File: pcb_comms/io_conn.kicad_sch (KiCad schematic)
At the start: 24 parts, among them IC1 CP2102N-A02-GQFN28, J1 Conn_01x06_Pin, J3 OBC_I2C, J4 Conn_01x04, J5 OBC_I2C, J6 Conn_01x04, J7 105164-0001, U6 ADP122AUJZ-3.3-R7

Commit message: Version 1.0. No DRA yet
From now on I will make the connections for IIS and then adapt it for the club
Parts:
- C39: value 10uF/25V(20%) -> 10uF
- R9: value 1k -> 1K
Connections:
- net GND: no longer J3.2 (Pin_2)
- new net OCP_NFAULT: J3.2 (Pin_2)
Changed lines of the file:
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@@
 	(wire
 		(pts
-			(xy 226.06 76.2) (xy 233.68 76.2)
+			(xy 227.33 76.2) (xy 233.68 76.2)
 		)
 		(stroke
@@
 		)
 	)
+	(global_label "OCP_NFAULT"
+		(shape input)
+		(at 227.33 76.2 180)
+		(fields_autoplaced yes)
+		(effects
+			(font
+				(size 1.27 1.27)
+			)
+			(justify right)
+		)
+		(property "Intersheetrefs" "${INTERSHEET_REFS}"
+			(at 212.6728 76.2 0)
+			(effects
+				(font
+					(size 1.27 1.27)
+				)
+				(justify right)
+				(hide yes)
+			)
+		)
+	)
 	(global_label "JTDO_SWO_TO_STM32"
 		(shape input)
@@
 			)
 		)
-		(property "Value" "1k"
+		(property "Value" "1K"
 			(at 111.76 182.8799 0)
 			(effects
@@
 		(dnp no)
 		(property "Reference" "C39"
-			(at 178.308 65.278 0)
+			(at 180.34 66.04 0)
 			(effects
 				(font
@@
 			)
 		)
-		(property "Value" "10uF/25V(20%)"
-			(at 176.53 79.502 90)
-			(effects
-				(font
-					(size 0.889 0.889)
+		(property "Value" "10uF"
+			(at 180.34 68.326 0)
+			(effects
+				(font
+					(size 1.27 1.27)
 				)
 				(justify left)
@@
 					(unit 1)
 				)
-			)
-		)
-	)
-	(symbol
-		(lib_id "power:GND")
-		(at 226.06 76.2 270)
-		(unit 1)
-		(exclude_from_sim no)
-		(in_bom yes)
-		(on_board yes)
-		(dnp no)
-		(fields_autoplaced yes)
-		(property "Reference" "#PWR060"
-			(at 219.71 76.2 0)
-			(effects
-				(font
-					(size 1.27 1.27)
-				)
-				(hide yes)
-			)
-		)
-		(property "Value" "GND"
-			(at 222.25 76.1999 90)
-			(effects
-				(font
-					(size 1.27 1.27)
-				)
-				(justify right)
-			)
-		)
-		(property "Footprint" ""
-			(at 226.06 76.2 0)
-			(effects
-				(font
-					(size 1.27 1.27)
-				)
-				(hide yes)
-			)
-		)
-		(property "Datasheet" ""
-			(at 226.06 76.2 0)
-			(effects
-				(font
-					(size 1.27 1.27)
-				)
-				(hide yes)
-			)
-		)
-		(property "Description" "Power symbol creates a global label with name \"GND\" , ground"
-			(at 226.06 76.2 0)
-			(effects
-				(font
-					(size 1.27 1.27)
-				)
-				(hide yes)
-			)
-		)
-		(pin "1"
-		)
-		(instances
-			(project "pcb_comms_board"
-				(path "/ea597178-b44d-4db9-826c-8f86e8d231f0/a4d41170-f1e3-4812-89ef-2aa6a238f022"
-					(reference "#PWR060")
-					(unit 1)
-				)

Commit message: Add footprints
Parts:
- removed J3, J5: OBC_I2C, symbol Connector_Generic:Conn_01x02
- removed J4, J6: Conn_01x04, symbol Connector_Generic:Conn_01x04
- added J2: Conn_02x20_Counter_Clockwise, Connector_PinSocket_2.54mm:PinSocket_2x20_P2.54mm_Vertical, symbol Connector_Generic:Conn_02x20_Counter_Clockwise
- added J3: Conn_01x04, Connector_PinSocket_2.54mm:PinSocket_1x05_P2.54mm_Vertical, symbol Connector_Generic:Conn_01x04
- C37, C38, C39, C40, C41, C48: footprint (none) -> Capacitor_SMD:C_0805_2012Metric_Pad1.18x1.45mm_HandSolder
- C47: footprint (none) -> Capacitor_SMD:C_1210_3225Metric_Pad1.33x2.70mm_HandSolder
- CR1, CR2: footprint (none) -> SCHOTTKY_DIODE_SD1206S040S1R0:SCHOTTKY_DIODE_SD1206S040S1R0
- D2: footprint (none) -> ESD_PROTECTION_DIODE_SP0503BAHTG:ESD_PROTECTION_DIODE_SP0503BAHTG
- D6: value Green -> GREEN; footprint (none) -> LED_SMD:LED_0805_2012Metric_Pad1.15x1.40mm_HandSolder
- IC1: footprint (none) -> USB_TO_UART_BRIDGE_CP2102N:USB_TO_UART_BRIDGE_CP2102N-A02-GQFN28
- J1: footprint (none) -> Connector_PinHeader_2.54mm:PinHeader_1x06_P2.54mm_Vertical_SMD_Pin1Right
- J7: value 105164-0001 -> USB-B-Micro; footprint (none) -> USB_RECEPTACLE_105164-0001_MOLEX:USB_RECEPTACLE_105164-0001
- R2, R3, R4: footprint (none) -> Resistor_SMD:R_0805_2012Metric_Pad1.20x1.40mm_HandSolder
- R9: footprint Resistor_SMD:R_0805_2012Metric -> Resistor_SMD:R_0805_2012Metric_Pad1.20x1.40mm_HandSolder
- SB3: footprint (none) -> Jumper:SolderJumper-2_P1.3mm_Open_RoundedPad1.0x1.5mm
- U6: footprint (none) -> LDO_ADP122AUJZ_3_3_R7:UJ_5_ADI
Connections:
- net GND: now also J2.11 (Pin_11), J2.12 (Pin_12), J2.13 (Pin_13), J2.14 (Pin_14), J2.17 (Pin_17), J2.18 (Pin_18), J2.21 (Pin_21), J2.22 (Pin_22), J2.27 (Pin_27), J2.28 (Pin_28), J2.3 (Pin_3), J2.37 (Pin_37), J2.38 (Pin_38), J2.39 (Pin_39), J2.4 (Pin_4), J2.40 (Pin_40)
- net OCP_EN: now also J2.30 (Pin_30)
- net SPI1_CS: now also J2.25 (Pin_25)
- net SPI1_MISO: now also J2.23 (Pin_23)
- net SPI1_MOSI: now also J2.26 (Pin_26)
- net SPI1_SCK: now also J2.24 (Pin_24)
- net SPI2_CS: now also J3.4 (Pin_4)
- net SPI2_MISO: now also J3.3 (Pin_3)
- net SPI2_MOSI: now also J3.2 (Pin_2)
- net SPI2_SCK: now also J3.1 (Pin_1)
- net VBAT_IN: now also J2.5 (Pin_5)
- no-connect marks 19 -> 37
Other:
- note added: "TO OBC"
- note removed: "CAN BUS (SPI)"
- note removed: "OBC"

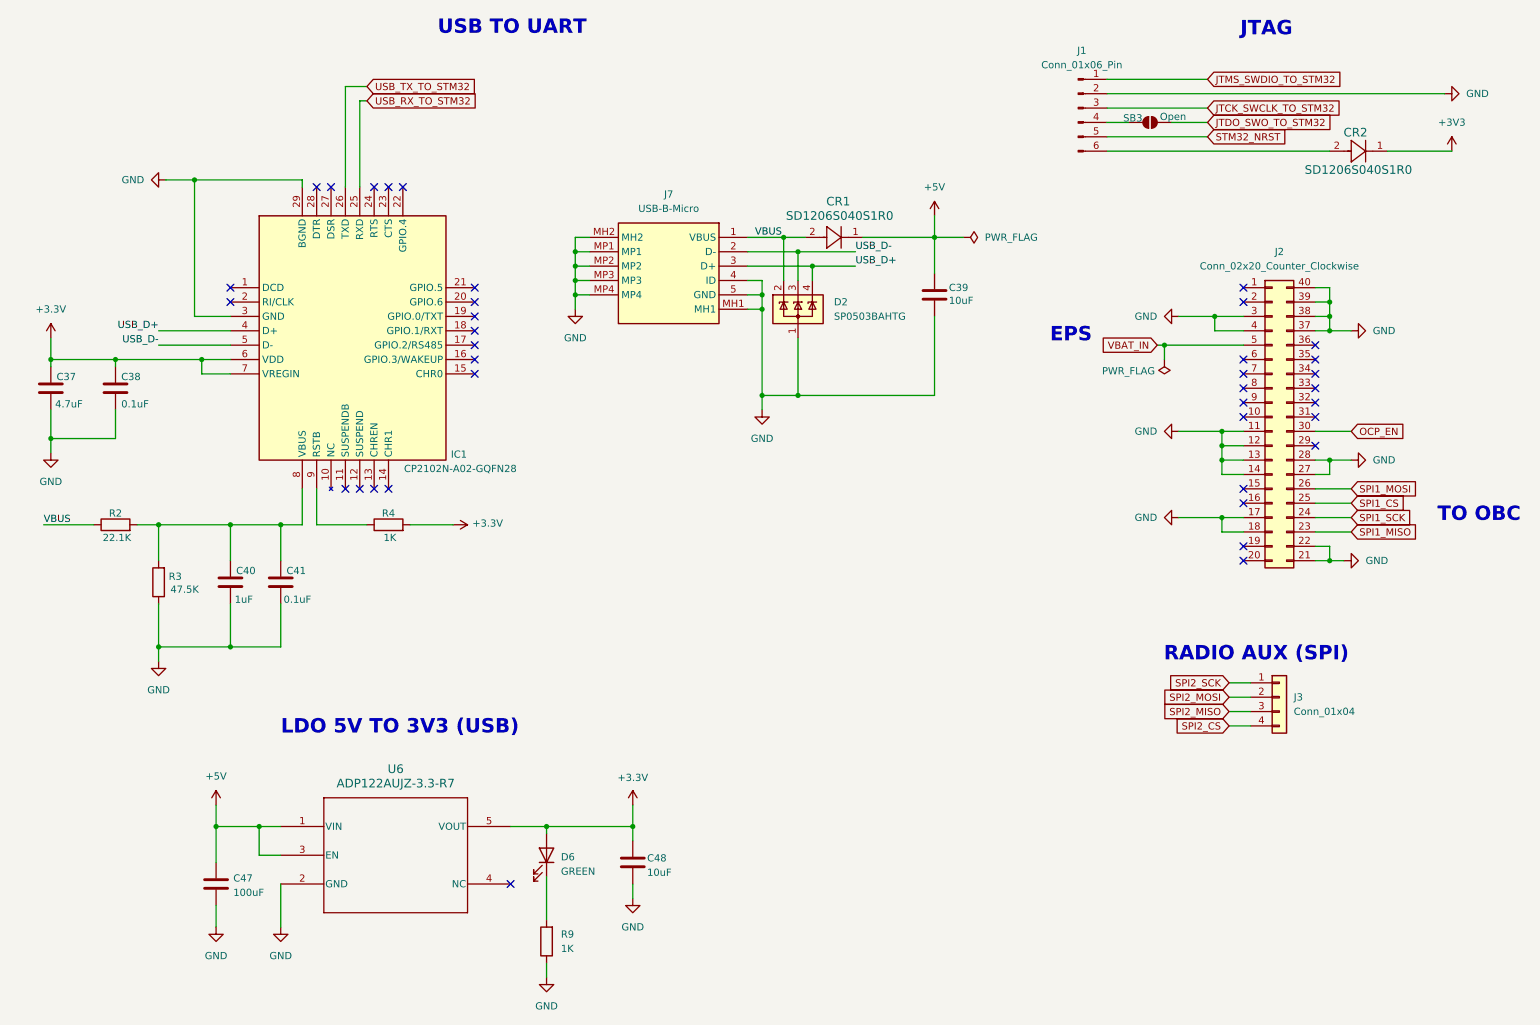
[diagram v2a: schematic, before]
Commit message: Add DRA818
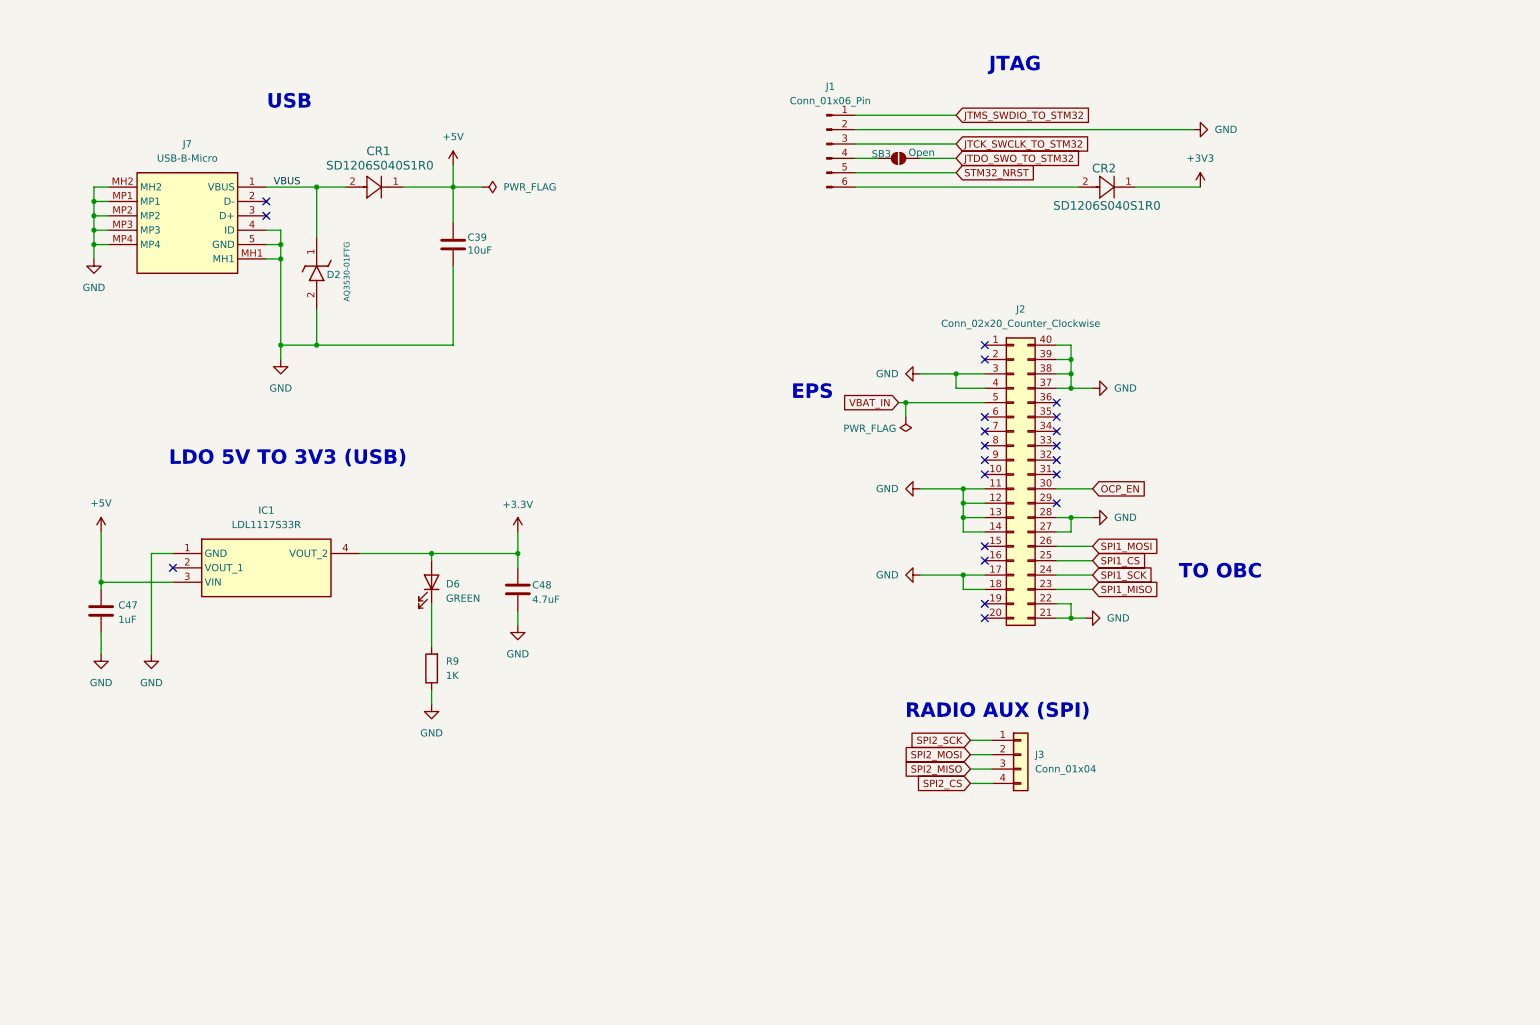
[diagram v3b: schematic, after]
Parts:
- removed C37: 4.7uF, Capacitor_SMD:C_0805_2012Metric_Pad1.18x1.45mm_HandSolder, symbol Device:C
- removed C38, C41: 0.1uF, Capacitor_SMD:C_0805_2012Metric_Pad1.18x1.45mm_HandSolder, symbol Device:C
- removed C40: 1uF, Capacitor_SMD:C_0805_2012Metric_Pad1.18x1.45mm_HandSolder, symbol Device:C
- removed D2: SP0503BAHTG, ESD_PROTECTION_DIODE_SP0503BAHTG:ESD_PROTECTION_DIODE_SP0503BAHTG, symbol Power_Protection:SP0503BAHT
- removed IC1: CP2102N-A02-GQFN28, USB_TO_UART_BRIDGE_CP2102N:USB_TO_UART_BRIDGE_CP2102N-A02-GQFN28, symbol USB_TO_UART_BRIDGE_CP2102N-A02-GQFN28:CP2102N-A02-GQFN28
- removed R2: 22.1K, Resistor_SMD:R_0805_2012Metric_Pad1.20x1.40mm_HandSolder, symbol Device:R
- removed R3: 47.5K, Resistor_SMD:R_0805_2012Metric_Pad1.20x1.40mm_HandSolder, symbol Device:R
- removed R4: 1K, Resistor_SMD:R_0805_2012Metric_Pad1.20x1.40mm_HandSolder, symbol Device:R
- removed U6: ADP122AUJZ-3.3-R7, LDO_ADP122AUJZ_3_3_R7:UJ_5_ADI, symbol LDO_ADP122AUJZ_3_3_R7:ADP122AUJZ-3.3-R7
- added D2: AQ3530-01FTG, ESD_PROTECTION_DIODE_AQ3530-01FTG:ESD_PROTECTION_DIODE_AQ3530-01FTG, symbol ESD_PROTECTION_DIODE_AQ3530-01FTG:AQ3530-01FTG
- added IC1: LDL1117S33R, LDO_LDL1117S33R:LDO_LDL1117S33R, symbol LDO_LDL1117S33R:LDL1117S33R
- C47: value 100uF -> 1uF; footprint Capacitor_SMD:C_1210_3225Metric_Pad1.33x2.70mm_HandSolder -> Capacitor_SMD:C_0805_2012Metric_Pad1.18x1.45mm_HandSolder
- C48: value 10uF -> 4.7uF
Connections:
- net +3.3V: now also IC1.4 (VOUT_2)
- net +5V: now also IC1.3 (VIN)
- net GND: now also D2.2 (A), IC1.1 (GND)
- net VBUS: now also D2.1 (K)
- net USB_D+: no longer names the net of J7.3 (D+)
- net USB_D-: no longer names the net of J7.2 (D-)
- no-connect marks 37 -> 21
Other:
- note added: "USB"
- note removed: "USB TO UART"
- moved on the sheet: C39, C47, C48, CR1, CR2, D6, J1, J2, J3, J7, R9, SB3

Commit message: remove gps
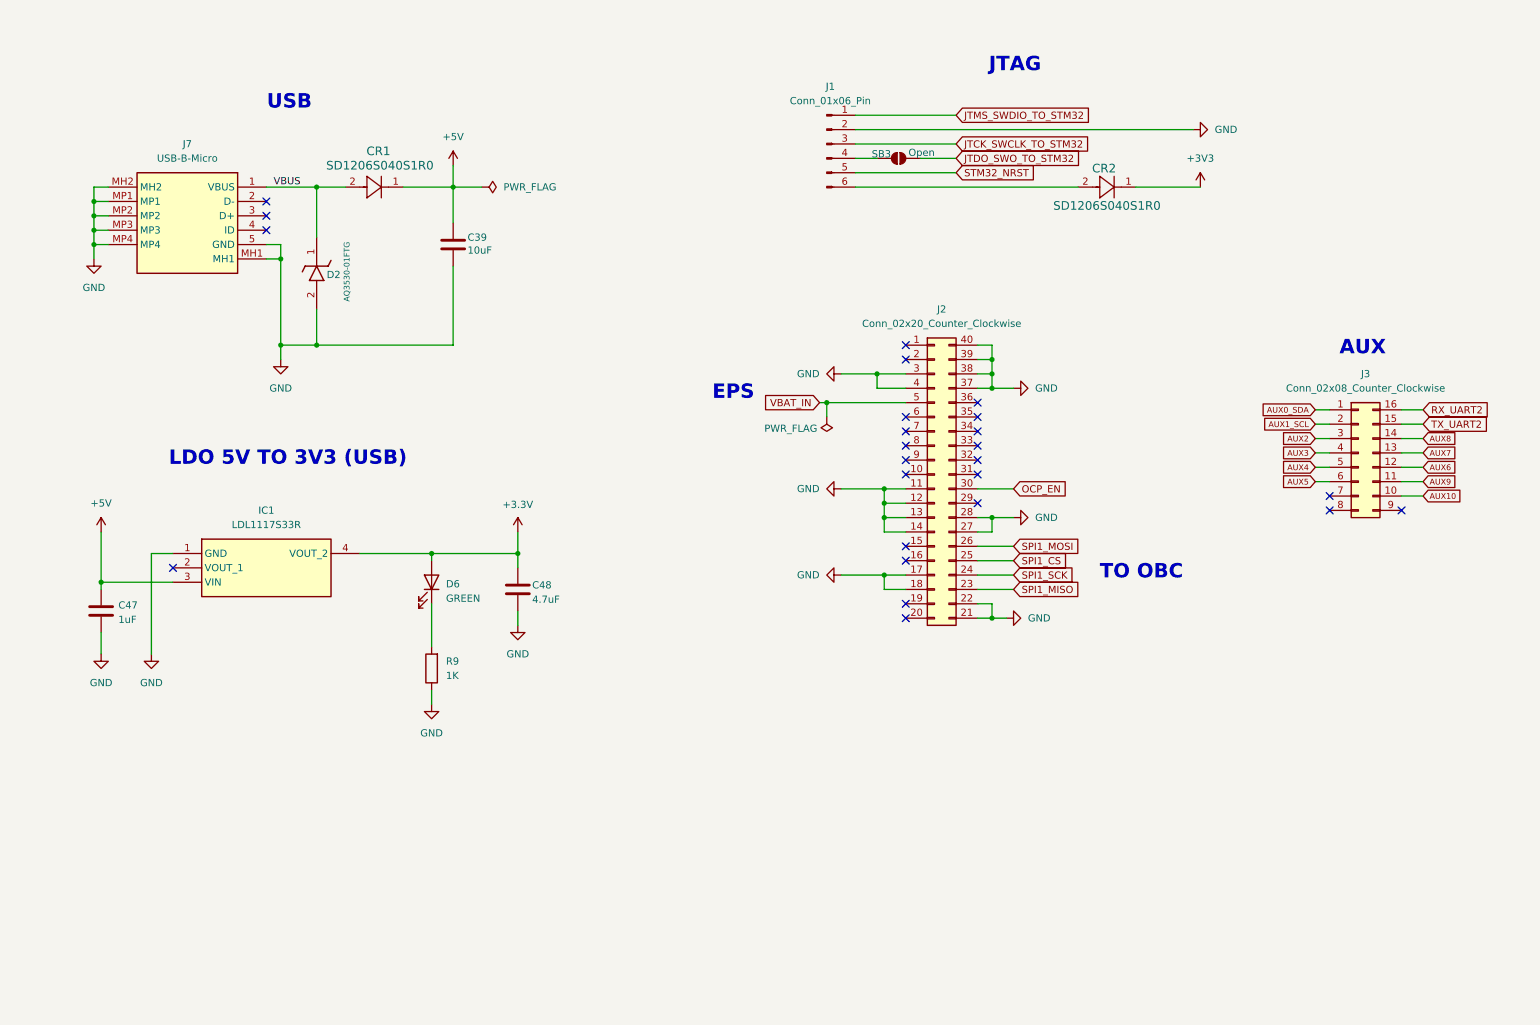
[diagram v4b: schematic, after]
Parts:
- removed J3: Conn_01x04, Connector_PinSocket_2.54mm:PinSocket_1x05_P2.54mm_Vertical, symbol Connector_Generic:Conn_01x04
- added J3: Conn_02x08_Counter_Clockwise, Connector_PinSocket_2.54mm:PinSocket_2x08_P2.54mm_Vertical_SMD, symbol Connector_Generic:Conn_02x08_Counter_Clockwise
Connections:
- net GND: no longer J7.4 (ID)
- new net AUX0_SDA: J3.1 (Pin_1)
- new net AUX10: J3.10 (Pin_10)
- new net AUX1_SCL: J3.2 (Pin_2)
- new net AUX2: J3.3 (Pin_3)
- new net AUX3: J3.4 (Pin_4)
- new net AUX4: J3.5 (Pin_5)
- new net AUX5: J3.6 (Pin_6)
- new net AUX6: J3.12 (Pin_12)
- new net AUX7: J3.13 (Pin_13)
- new net AUX8: J3.14 (Pin_14)
- new net AUX9: J3.11 (Pin_11)
- new net RX_UART2: J3.16 (Pin_16)
- new net TX_UART2: J3.15 (Pin_15)
- no-connect marks 21 -> 25
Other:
- note added: "AUX"
- note removed: "RADIO AUX (SPI)"
- moved on the sheet: J2

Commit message: Add UART USB
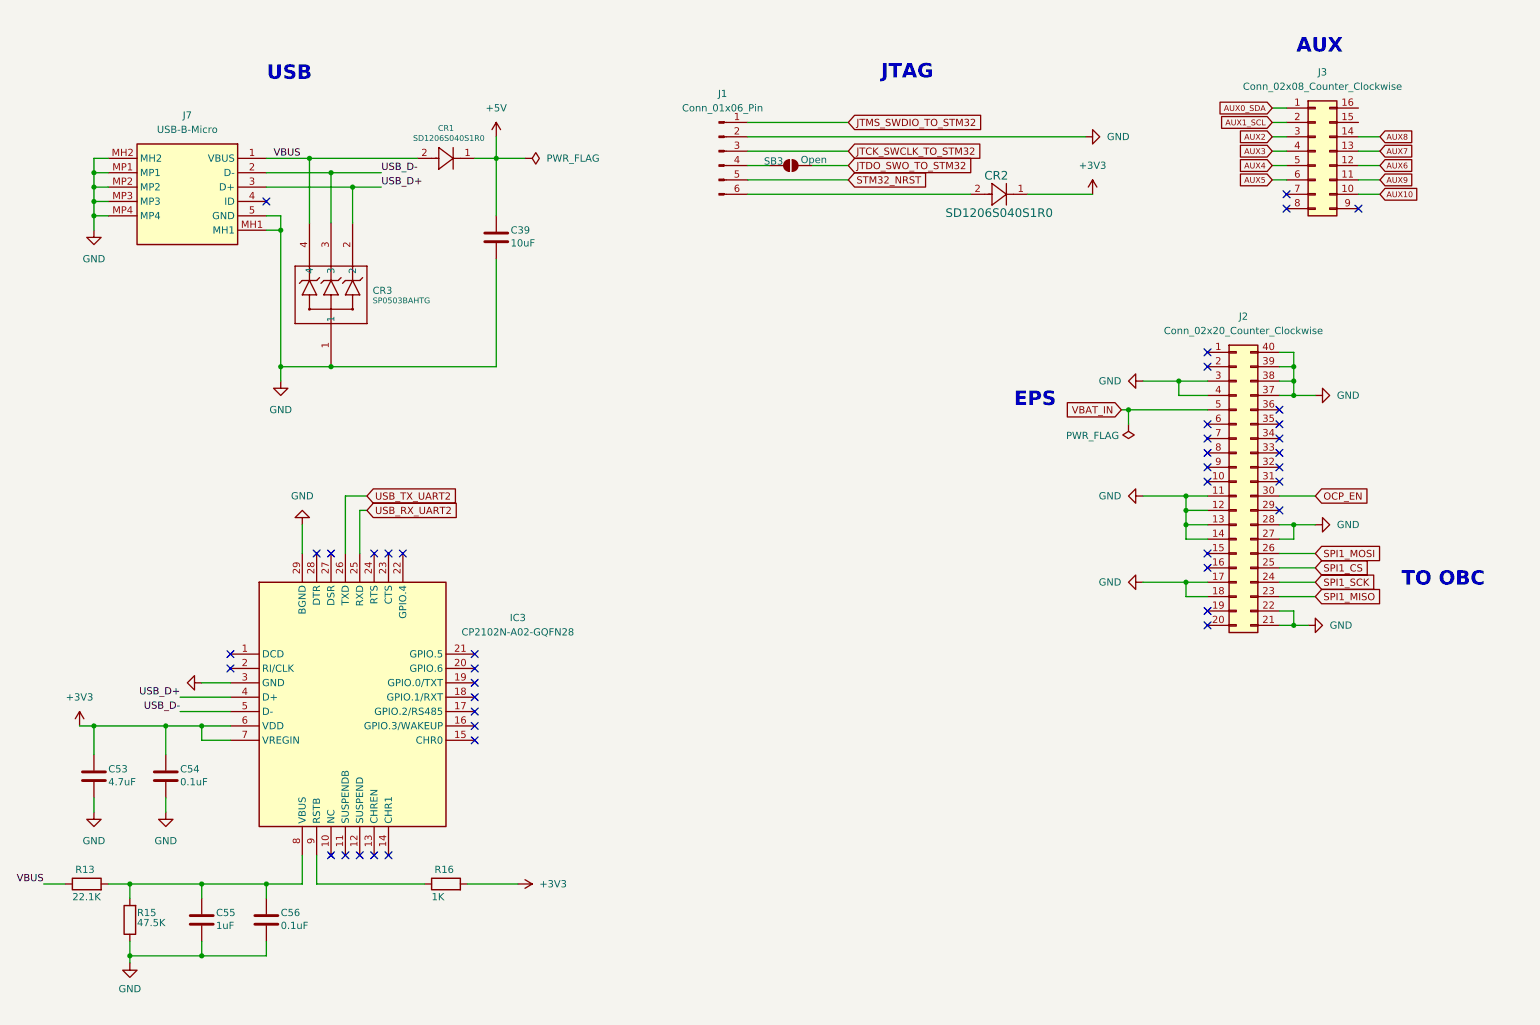
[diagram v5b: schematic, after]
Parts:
- removed C47: 1uF, Capacitor_SMD:C_0805_2012Metric_Pad1.18x1.45mm_HandSolder, symbol Device:C
- removed C48: 4.7uF, Capacitor_SMD:C_0805_2012Metric_Pad1.18x1.45mm_HandSolder, symbol Device:C
- removed D2: AQ3530-01FTG, ESD_PROTECTION_DIODE_AQ3530-01FTG:ESD_PROTECTION_DIODE_AQ3530-01FTG, symbol ESD_PROTECTION_DIODE_AQ3530-01FTG:AQ3530-01FTG
- removed D6: GREEN, LED_SMD:LED_0805_2012Metric_Pad1.15x1.40mm_HandSolder, symbol Device:LED
- removed IC1: LDL1117S33R, LDO_LDL1117S33R:LDO_LDL1117S33R, symbol LDO_LDL1117S33R:LDL1117S33R
- removed R9: 1K, Resistor_SMD:R_0805_2012Metric_Pad1.20x1.40mm_HandSolder, symbol Device:R
- added C53: 4.7uF, Capacitor_SMD:C_0805_2012Metric_Pad1.18x1.45mm_HandSolder, symbol Device:C
- added C54, C56: 0.1uF, Capacitor_SMD:C_0805_2012Metric_Pad1.18x1.45mm_HandSolder, symbol Device:C
- added C55: 1uF, Capacitor_SMD:C_0805_2012Metric_Pad1.18x1.45mm_HandSolder, symbol Device:C
- added CR3: SP0503BAHTG, ESD_PROTECTION_DIODE_SP0503BAHTG:ESD_PROTECTION_DIODE_SP0503BAHTG, symbol ESD_PROTECTION_DIODE_SP0503BAHTG:SP0503BAHTG
- added IC3: CP2102N-A02-GQFN28, USB_TO_UART_BRIDGE_CP2102N:USB_TO_UART_BRIDGE_CP2102N-A02-GQFN28, symbol USB_TO_UART_BRIDGE_CP2102N-A02-GQFN28:CP2102N-A02-GQFN28
- added R13: 22.1K, Resistor_SMD:R_0805_2012Metric_Pad1.20x1.40mm_HandSolder, symbol Device:R
- added R15: 47.5K, Resistor_SMD:R_0805_2012Metric_Pad1.20x1.40mm_HandSolder, symbol Device:R
- added R16: 1K, Resistor_SMD:R_0805_2012Metric_Pad1.20x1.40mm_HandSolder, symbol Device:R
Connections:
- net +3V3: now also C53.1, C54.1, IC3.6 (VDD), IC3.7 (VREGIN), R16.2
- net GND: now also C53.2, C54.2, C55.2, C56.2, CR3.1, IC3.29 (BGND), IC3.3 (GND), R15.1
- net VBUS: now also CR3.4, R13.1
- net USB_D-: now reaches J7.2 (D-)
- net USB_D-: now also CR3.3, IC3.5 (D-)
- net USB_D+: now reaches J7.3 (D+)
- net USB_D+: now also CR3.2, IC3.4 (D+)
- net RX_UART2: no longer names the net of J3.16 (Pin_16)
- net TX_UART2: no longer names the net of J3.15 (Pin_15)
- new net: C55.1, C56.1, IC3.8 (VBUS), R13.2, R15.2
- new net: IC3.9 (RSTB), R16.1
- new net USB_RX_UART2: IC3.25 (RXD)
- new net USB_TX_UART2: IC3.26 (TXD)
- no-connect marks 25 -> 41
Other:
- note removed: "LDO 5V TO 3V3 (USB)"
- moved on the sheet: C39, CR1, CR2, J1, J2, J3, J7, SB3
